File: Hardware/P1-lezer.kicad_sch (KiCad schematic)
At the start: 9 parts, among them J1 RJ12, Q1 BC547, U1 WeMos_D1_mini, U2 TIL111

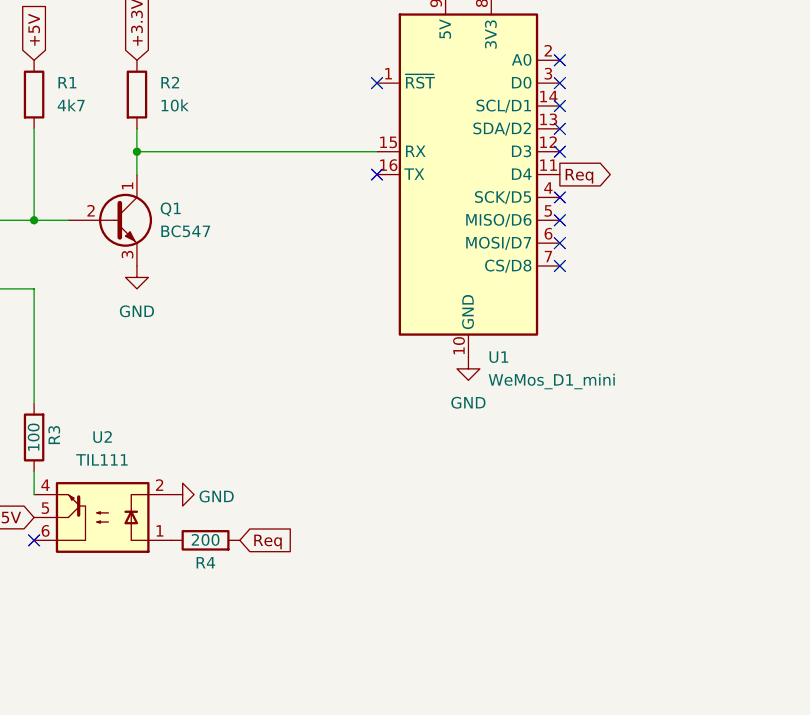
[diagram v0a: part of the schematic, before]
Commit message: Moved the request output from D4 to D5.
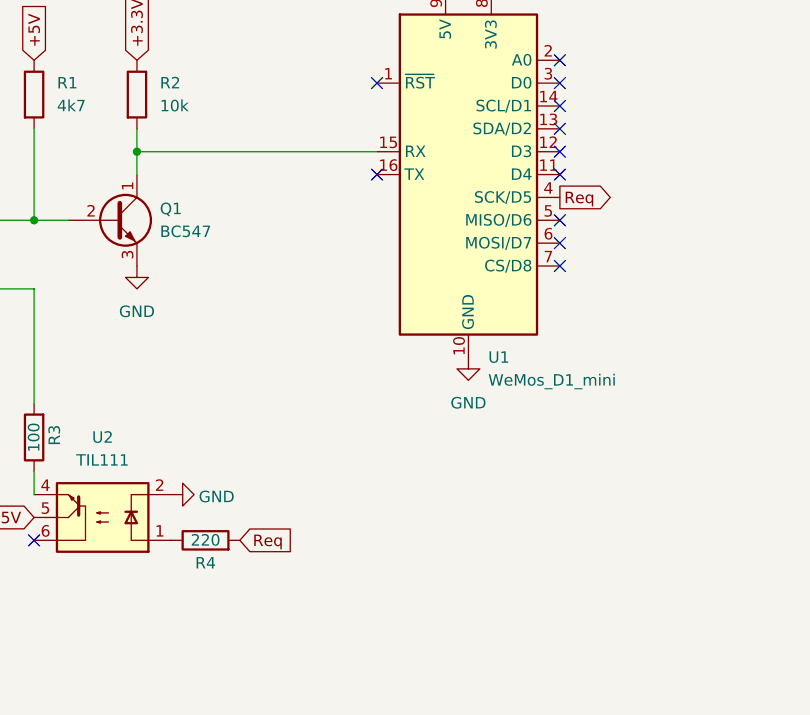
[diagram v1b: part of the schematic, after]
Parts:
- R4: value 200 -> 220
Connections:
- net Req: now also U1.4 (SCK/D5); no longer U1.11 (D4)
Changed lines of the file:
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@@
+	)
+	(no_connect
+		(at 190.5 81.28)
 	)
 	(no_connect
@@
 	(no_connect
 		(at 190.5 91.44)
-	)
-	(no_connect
-		(at 190.5 83.82)
 	)
 	(no_connect
@@
 	(global_label "Req"
 		(shape output)
-		(at 190.5 81.28 0)
+		(at 190.5 83.82 0)
 		(fields_autoplaced yes)
 		(effects
@@
 		)
 		(property "Intersheetrefs" "${INTERSHEET_REFS}"
-			(at 196.9928 81.28 0)
+			(at 196.9928 83.82 0)
 			(effects
 				(font
@@
 			)
 		)
-		(property "Value" "200"
+		(property "Value" "220"
 			(at 151.13 121.92 90)
 			(effects
@@
 			(at 151.13 121.92 0)
 			(effects
+				(font
+					(size 1.27 1.27)
+				)
+				(hide yes)
+			)
+		)
+		(property "Untitled Field" ""
+			(at 151.13 121.92 0)
+			(effects

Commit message: Moved request line to D1 and rerouted the board to match this change.
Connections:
- net Req: now also U1.14 (SCL/D1); no longer U1.4 (SCK/D5)
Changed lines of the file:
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@@
-	)
-	(no_connect
-		(at 190.5 73.66)
 	)
 	(no_connect
@@
 	(no_connect
 		(at 190.5 86.36)
+	)
+	(no_connect
+		(at 190.5 83.82)
 	)
 	(no_connect
@@
 	(global_label "Req"
 		(shape output)
-		(at 190.5 83.82 0)
-		(fields_autoplaced yes)
-		(effects
-			(font
-				(size 1.27 1.27)
-			)
-			(justify left)
-		)
-		(property "Intersheetrefs" "${INTERSHEET_REFS}"
-			(at 196.9928 83.82 0)
-			(effects
-				(font
+		(at 190.5 73.66 0)
+		(fields_autoplaced yes)
+		(effects
+			(font
+				(size 1.27 1.27)
+			)
+			(justify left)
+		)
+		(property "Intersheetrefs" "${INTERSHEET_REFS}"
+			(at 196.9928 73.66 0)
+			(effects
+				(font

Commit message: Optocoupler aangepast naar CNY17-1
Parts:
- removed U2: TIL111, Package_DIP:DIP-6_W7.62mm, symbol Isolator:TIL111
- added U2: CNY17-1, Package_DIP:DIP-6_W7.62mm, symbol Isolator:CNY17-1
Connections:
- net +5V: now also U2.5
- net GND: now also U2.2
- net at R4.1: now also U2.1
- net at R3.1: now also U2.4
